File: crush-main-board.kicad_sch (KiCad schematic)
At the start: 37 parts, among them J1 4x4_Header, J10 3x3 Header, J11 3x3 Header, J12 3x2 Header, J13 3x4_Header, J14 3x4_Header, J15 2157601008, J16 Conn_01x02, J17 Conn_01x02, J2 4x4_Header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

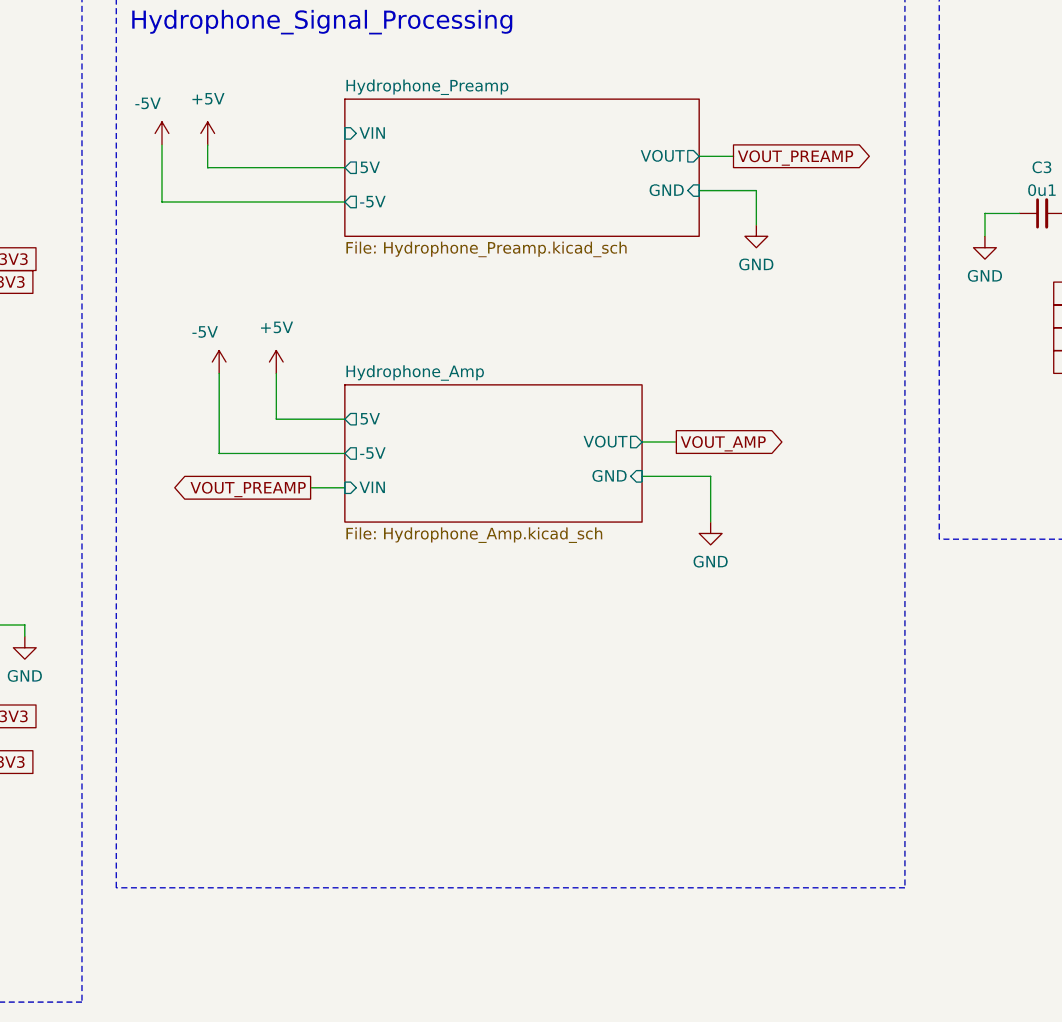
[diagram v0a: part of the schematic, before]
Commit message: Add hydrophone filter sim circuit and subsheet (Stage 3)
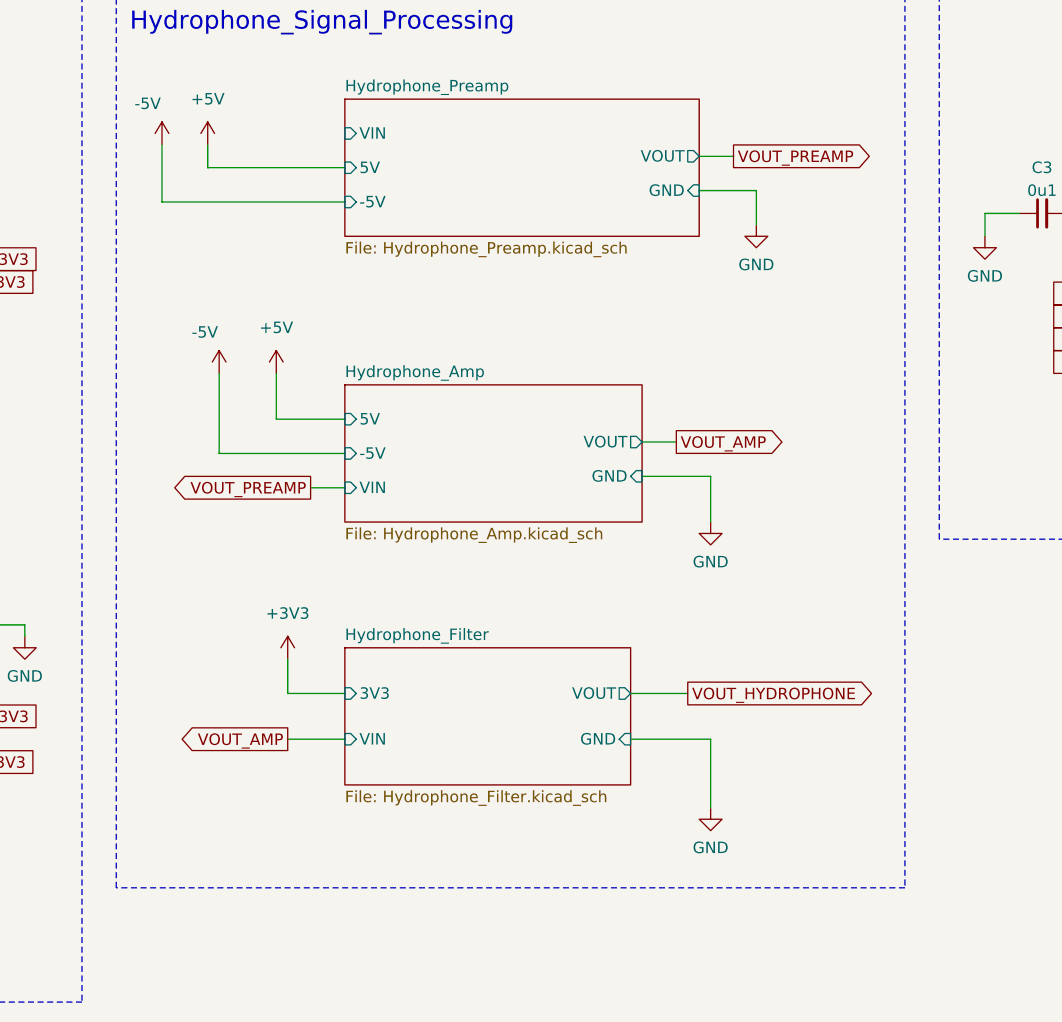
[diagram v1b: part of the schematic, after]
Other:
- added sheet Hydrophone_Filter (Hydrophone_Filter.kicad_sch)

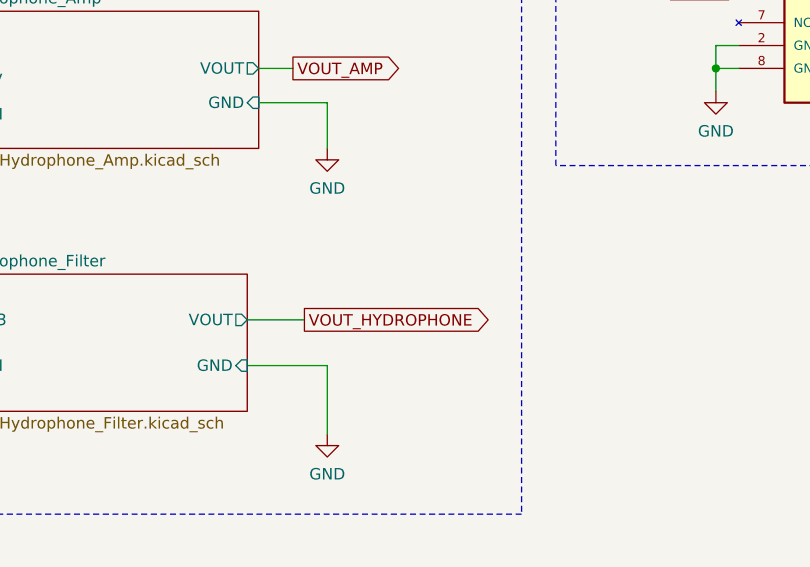
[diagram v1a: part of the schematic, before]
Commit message: Added footprints and ROUGH PCB placements/routing
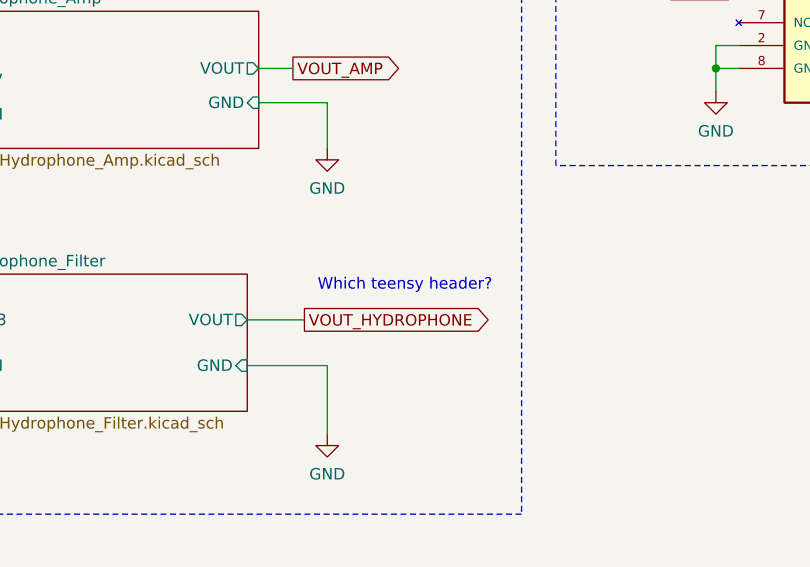
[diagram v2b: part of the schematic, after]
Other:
- note added: "Which teensy header?"
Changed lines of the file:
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@@
+		)
+	)
+	(text "Which teensy header?"
+		(exclude_from_sim no)
+		(at 315.976 116.84 0)
+		(effects
+			(font
+				(size 1.27 1.27)
+			)
 		)
 	)

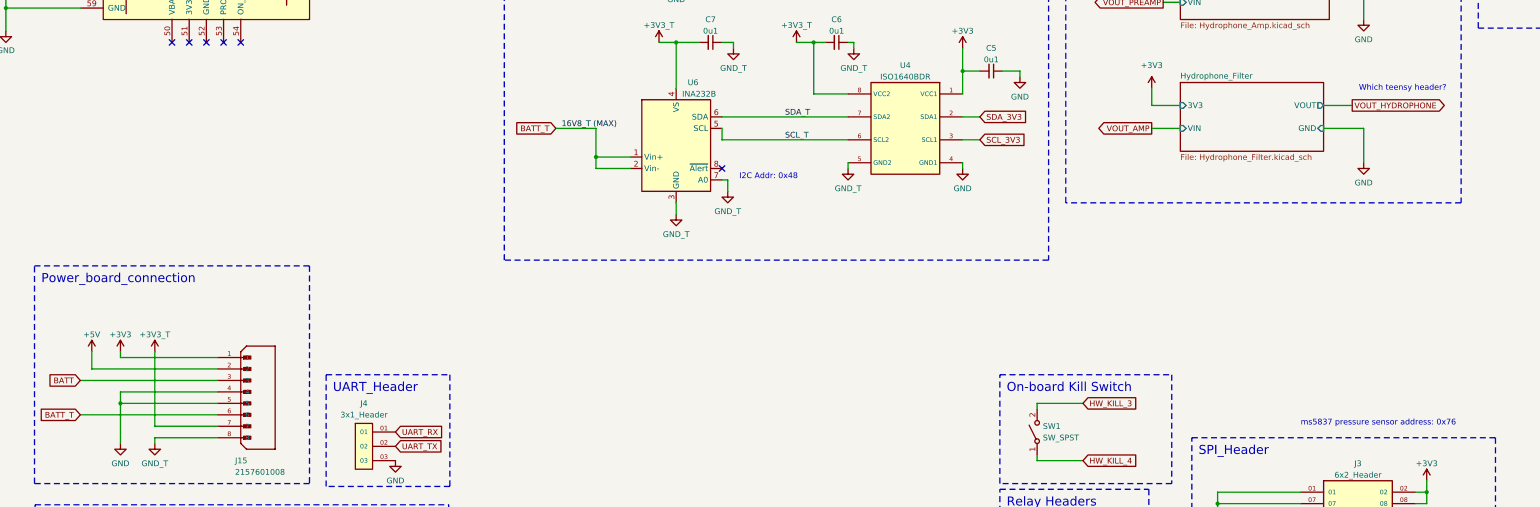
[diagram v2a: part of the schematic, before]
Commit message: Add -5V pin (pin 4) to power board connection
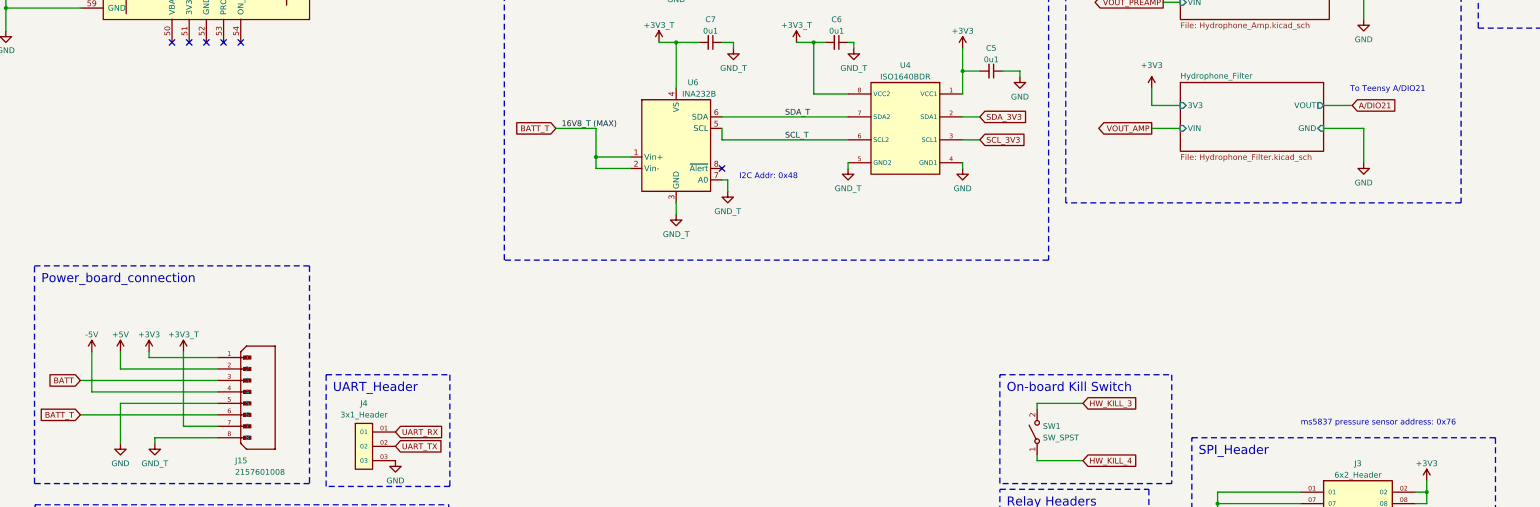
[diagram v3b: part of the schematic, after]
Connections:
- net -5V: now also J15.4
- net GND: no longer J15.4
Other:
- note added: "To Teensy A/DIO21"
- note removed: "Which teensy header?"
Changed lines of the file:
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@@
 		)
 	)
-	(text "Which teensy header?"
+	(text "To Teensy A/DIO21"
 		(exclude_from_sim no)
-		(at 315.976 116.84 0)
+		(at 312.674 117.094 0)
 		(effects
 			(font
@@
 	)
 	(junction
-		(at 31.75 186.69)
-		(diameter 0)
-		(color 0 0 0 0)
-	)
-	(junction
 		(at 386.08 45.085)
 		(diameter 0)
@@
 	(wire
 		(pts
+			(xy 53.34 184.15) (xy 25.4 184.15)
+		)
+		(stroke
+			(width 0)
+			(type default)
+		)
+	)
+	(wire
+		(pts
 			(xy 269.875 262.89) (xy 269.875 265.43)
 		)
@@
 	(wire
 		(pts
-			(xy 31.75 176.53) (xy 31.75 175.26)
+			(xy 38.1 176.53) (xy 38.1 175.26)
 		)
 		(stroke
@@
 	(wire
 		(pts
-			(xy 53.34 184.15) (xy 31.75 184.15)
-		)
-		(stroke
-			(width 0)
-			(type default)
-		)
-	)
-	(wire
-		(pts
 			(xy 78.74 19.05) (xy 86.995 19.05)
 		)
@@
 	(wire
 		(pts
-			(xy 39.37 191.77) (xy 39.37 175.26)
+			(xy 45.72 191.77) (xy 45.72 175.26)
 		)
 		(stroke
@@
 	(wire
 		(pts
-			(xy 31.75 184.15) (xy 31.75 186.69)
-		)
-		(stroke
-			(width 0)
-			(type default)
-		)
-	)
-	(wire
-		(pts
 			(xy 320.675 250.19) (xy 318.135 250.19)
 		)
@@
 	(wire
 		(pts
+			(xy 25.4 184.15) (xy 25.4 175.26)
+		)
+		(stroke
+			(width 0)
+			(type default)
+		)
+	)
+	(wire
+		(pts
 			(xy 78.74 21.59) (xy 92.075 21.59)
 		)
@@
 	(wire
 		(pts
-			(xy 25.4 175.26) (xy 25.4 179.07)
+			(xy 31.75 175.26) (xy 31.75 179.07)
 		)
 		(stroke
@@
 	(wire
 		(pts
-			(xy 53.34 176.53) (xy 31.75 176.53)
+			(xy 53.34 176.53) (xy 38.1 176.53)
 		)
 		(stroke
@@
 	(wire
 		(pts
-			(xy 25.4 179.07) (xy 53.34 179.07)
+			(xy 31.75 179.07) (xy 53.34 179.07)
 		)
 		(stroke
@@
 	(wire
 		(pts
-			(xy 53.34 191.77) (xy 39.37 191.77)
+			(xy 53.34 191.77) (xy 45.72 191.77)
 		)
 		(stroke
@@
 		)
 	)
-	(global_label "VOUT_HYDROPHONE"
-		(shape output)
+	(global_label "A{slash}DIO21"
+		(shape input)
 		(at 304.8 120.65 0)
 		(fields_autoplaced yes)
@@
 		)
 		(property "Intersheetrefs" "${INTERSHEET_REFS}"
-			(at 326.1701 120.65 0)
+			(at 315.8286 120.65 0)
 			(hide yes)
 			(show_name no)
@@
 	(symbol
 		(lib_id "power:+3V3")
-		(at 31.75 175.26 0)
+		(at 38.1 175.26 0)
 		(unit 1)
 		(body_style 1)
@@
 		(fields_autoplaced yes)
 		(property "Reference" "#PWR057"
-			(at 31.75 179.07 0)
+			(at 38.1 179.07 0)
 			(hide yes)
 			(show_name no)
@@
 		)
 		(property "Value" "+3V3"
-			(at 31.75 171.45 0)
+			(at 38.1 171.45 0)
 			(show_name no)
 			(do_not_autoplace no)
@@
 		)
 		(property "Footprint" ""
-			(at 31.75 175.26 0)
+			(at 38.1 175.26 0)
 			(hide yes)
 			(show_name no)
@@
 		)
 		(property "Datasheet" ""
-			(at 31.75 175.26 0)
+			(at 38.1 175.26 0)
 			(hide yes)
 			(show_name no)
@@
 		)
 		(property "Description" ""
-			(at 31.75 175.26 0)
+			(at 38.1 175.26 0)
 			(show_name no)
 			(do_not_autoplace no)
@@
 	)
 	(symbol
+		(lib_id "power:+5V")
+		(at 25.4 175.26 0)
+		(mirror y)
+		(unit 1)
+		(body_style 1)
+		(exclude_from_sim yes)
+		(in_bom yes)
+		(on_board yes)
+		(in_pos_files yes)
+		(dnp no)
+		(fields_autoplaced yes)
+		(property "Reference" "#PWR082"
+			(at 25.4 179.07 0)
+			(hide yes)
+			(show_name no)
+			(do_not_autoplace no)
+			(effects
+				(font
+					(size 1.27 1.27)
+				)
+			)
+		)
+		(property "Value" "-5V"
+			(at 25.4 171.45 0)
+			(show_name no)
+			(do_not_autoplace no)
+			(effects
+				(font
+					(size 1.27 1.27)
+				)
+			)
+		)
+		(property "Footprint" ""
+			(at 25.4 175.26 0)
+			(hide yes)
+			(show_name no)
+			(do_not_autoplace no)
+			(effects
+				(font
+					(size 1.27 1.27)
+				)
+			)
+		)
+		(property "Datasheet" ""
+			(at 25.4 175.26 0)
+			(hide yes)
+			(show_name no)
+			(do_not_autoplace no)
+			(effects
+				(font
+					(size 1.27 1.27)
+				)
+			)
+		)
+		(property "Description" ""
+			(at 25.4 175.26 0)
+			(show_name no)
+			(do_not_autoplace no)
+			(effects
+				(font
+					(size 1.27 1.27)
+				)
+			)
+		)
+		(pin "1"
+		)
+		(instances
+			(project "crush-main-board"
+				(path "/74b566fe-9d71-4817-95ed-d472d647f8c8"
+					(reference "#PWR082")
+					(unit 1)
+				)
+			)
+		)
+	)
+	(symbol
 		(lib_id "Mechanical:MountingHole_Pad")
 		(at 382.27 139.7 270)
@@
 	(symbol
 		(lib_id "Crush_MainBoard_Symbols:+3V3_T")
-		(at 39.37 175.26 0)
+		(at 45.72 175.26 0)
 		(unit 1)
 		(body_style 1)
@@
 		(fields_autoplaced yes)
 		(property "Reference" "#PWR052"
-			(at 39.37 179.07 0)
+			(at 45.72 179.07 0)
 			(hide yes)
 			(show_name no)
@@
 		)
 		(property "Value" "+3V3_T"
-			(at 39.37 171.45 0)
+			(at 45.72 171.45 0)
 			(show_name no)
 			(do_not_autoplace no)
@@
 		)
 		(property "Footprint" ""
-			(at 39.37 175.26 0)
+			(at 45.72 175.26 0)
 			(hide yes)
 			(show_name no)
@@
 		)
 		(property "Datasheet" ""
-			(at 39.37 175.26 0)
+			(at 45.72 175.26 0)
 			(hide yes)
 			(show_name no)
@@
 		)
 		(property "Description" ""
-			(at 39.37 175.26 0)
+			(at 45.72 175.26 0)
 			(show_name no)
 			(do_not_autoplace no)
@@
 	(symbol
 		(lib_id "power:+5V")
-		(at 25.4 175.26 0)
+		(at 31.75 175.26 0)
 		(mirror y)
 		(unit 1)
@@
 		(fields_autoplaced yes)
 		(property "Reference" "#PWR056"
-			(at 25.4 179.07 0)
+			(at 31.75 179.07 0)
 			(hide yes)
 			(show_name no)
@@
 		)
 		(property "Value" "+5V"
-			(at 25.4 171.45 0)
+			(at 31.75 171.45 0)
 			(show_name no)
 			(do_not_autoplace no)
@@
 		)
 		(property "Footprint" ""
-			(at 25.4 175.26 0)
+			(at 31.75 175.26 0)
 			(hide yes)
 			(show_name no)
@@
 		)
 		(property "Datasheet" ""
-			(at 25.4 175.26 0)
+			(at 31.75 175.26 0)
 			(hide yes)
 			(show_name no)
@@
 		)
 		(property "Description" ""
-			(at 25.4 175.26 0)
+			(at 31.75 175.26 0)
 			(show_name no)
 			(do_not_autoplace no)
